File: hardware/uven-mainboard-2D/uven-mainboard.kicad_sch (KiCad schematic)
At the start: 38 parts, among them J1 TEMP_LED0, J10 TEMP_SPECIMEN, J11 TEC1_COOLER, J12 TEC2_COOLER, J13 DISPLAY, J14 DISPLAY, J15 TEC3_COOLER, J16 MENU_BUTTON, J18 BUTTON0, J19 BUTTON1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

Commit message: pcb ordered in aisler
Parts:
- removed J10: TEMP_SPECIMEN, Connector_PinSocket_1.27mm:PinSocket_1x02_P1.27mm_Vertical, symbol uven-mainboard-rescue:Conn_01x02_Female-Connector
- removed J8: TEMP_LED0, Connector_PinSocket_1.27mm:PinSocket_1x02_P1.27mm_Vertical, symbol uven-mainboard-rescue:Conn_01x02_Female-Connector
- removed J9: TEMP_LED1, Connector_PinSocket_1.27mm:PinSocket_1x02_P1.27mm_Vertical, symbol uven-mainboard-rescue:Conn_01x02_Female-Connector
- removed TH1, TH2, TH3: 10k, Resistor_SMD:R_0603_1608Metric_Pad1.05x0.95mm_HandSolder, symbol uven-mainboard-rescue:Thermistor_NTC-Device
- added H1, H4, H6: GND, MountingHole:MountingHole_3.2mm_M3_DIN965_Pad_TopBottom, symbol Mechanical:MountingHole_Pad
- added H2, H3, H5: 12V, MountingHole:MountingHole_3.2mm_M3_DIN965_Pad_TopBottom, symbol Mechanical:MountingHole_Pad
- added J10: LED1_CONTROL, Connector_PinHeader_2.54mm:PinHeader_1x05_P2.54mm_Vertical, symbol Connector:Conn_01x05_Male
- added J8: ST7789_ISP_DISPLAY, Connector_PinHeader_2.54mm:PinHeader_1x07_P2.54mm_Vertical, symbol Connector:Conn_01x07_Male
- added J9: LED0_CONTROL, Connector_PinHeader_2.54mm:PinHeader_1x05_P2.54mm_Vertical, symbol Connector:Conn_01x05_Male
- U1, U2, U3: footprint (none) -> custom_lib:BTS3011
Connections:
- net KILL_0 is gone; now on net KILL0: J22.2 (Pin_2)
- net TEMP_SPECISMEN is gone; now on net TEMP_SPECIMEN: J3.1 (Pin_1), R3.1
- net +12V: now also J4.2 (Pin_2), J5.2 (Pin_2), H2.1, H3.1, H5.1
- net +3V3: now also J10.2 (Pin_2), J8.2 (Pin_2), J9.2 (Pin_2)
- net GND: now also H1.1, H4.1, H6.1, J10.1 (Pin_1), J8.1 (Pin_1), J9.1 (Pin_1); no longer J4.1 (Pin_1), J5.1 (Pin_1)
- net KILL0: now also XA1.D28; no longer XA1.D38
- net MENU_BUTTON: now also XA1.D11
- net MENU_CLK: now also XA1.D13
- net MENU_DT: now also XA1.D12
- net TEC_COOLER_IN: now also XA1.D2; no longer XA1.D4 (D4_CS1)
- net TEC_COOLER_STATUS: now also XA1.D5; no longer XA1.D7
- net TEC_LED0_IN: now also XA1.D4 (D4_CS1); no longer XA1.D2
- net TEC_LED0_STATUS: now also XA1.D7; no longer XA1.D5
- net LED0_ON/OFF: now reaches XA1.D14 (D14_TX3)
- net LED0_ON/OFF: now also J9.5 (Pin_5)
- net LED1_ON/OFF: now reaches XA1.D15 (D15_RX3)
- net LED1_ON/OFF: now also J10.5 (Pin_5)
- net LED0_I2C_SDA: now reaches XA1.D20 (D20_SDA)
- net LED0_I2C_SDA: now also J9.4 (Pin_4)
- net LED0_I2C_SCL: now reaches XA1.D21 (D21_SCL)
- net LED0_I2C_SCL: now also J9.3 (Pin_3)
- net ISP_RES: now reaches XA1.D35
- net ISP_RES: now also J8.5 (Pin_5)
- net ISP_DC: now reaches XA1.D36
- net ISP_DC: now also J8.6 (Pin_6)
- net ISP_BLK: now reaches XA1.D37
- net ISP_BLK: now also J8.7 (Pin_7)
- net LED1_I2C_SCL: now reaches XA1.SCL1
- net LED1_I2C_SCL: now also J10.3 (Pin_3)
- net LED1_I2C_SDA: now reaches XA1.SDA1
- net LED1_I2C_SDA: now also J10.4 (Pin_4)
- net at J11.1 (Pin_1), J12.1 (Pin_1), J15.1 (Pin_1)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: no longer U2.3 (OUT)
- net MISO renamed SPI_MISO
- net MOSI renamed SPI_MOSI
- net SPI_MOSI: now also J8.4 (Pin_4)
- net SCK renamed SPI_SCK
- net SPI_SCK: now also J8.3 (Pin_3)
- new net: J5.1 (Pin_1), U3.6 (OUT)
- new net: J4.1 (Pin_1), U1.6 (OUT)
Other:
- moved on the sheet: J1, J14, J2, J3, J4, R1, R2, R3, XA1

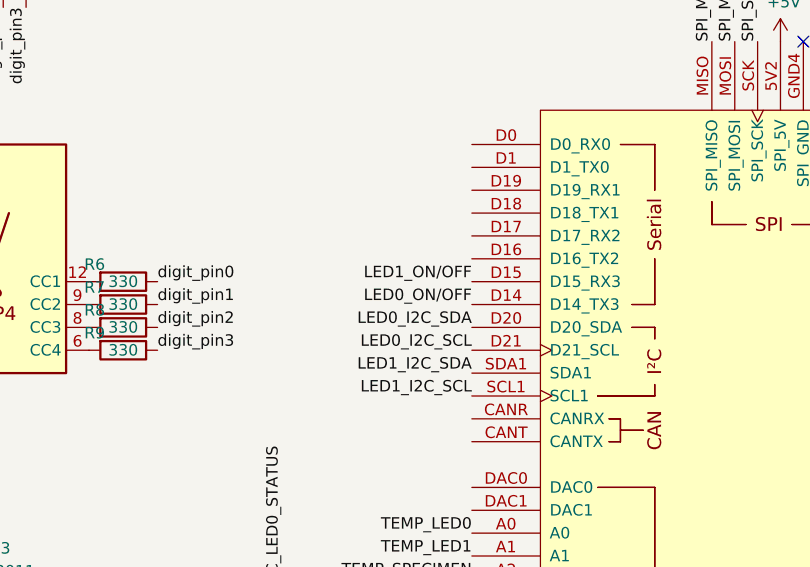
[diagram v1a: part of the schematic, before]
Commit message: uven pocket layout almost finished
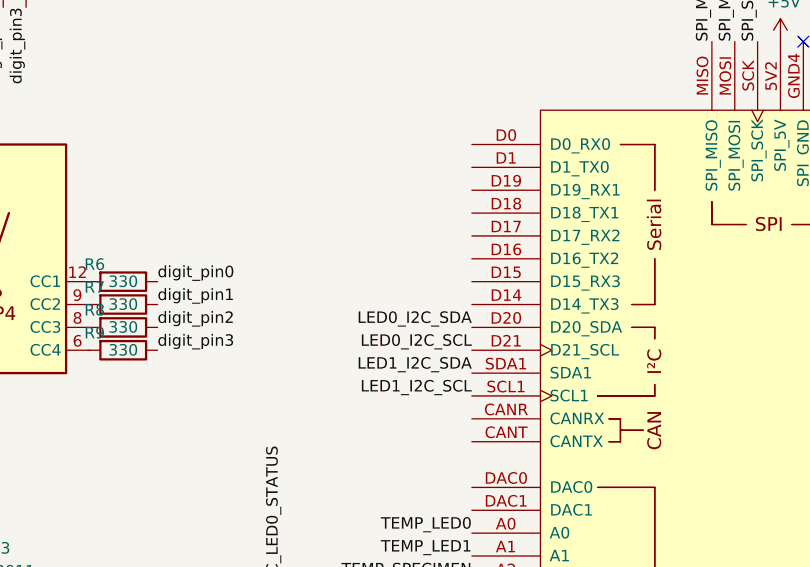
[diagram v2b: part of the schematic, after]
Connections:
- net LED0_ON/OFF: no longer XA1.D14 (D14_TX3)
- net LED1_ON/OFF: no longer XA1.D15 (D15_RX3)
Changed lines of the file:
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@@
     (effects (font (size 1.27 1.27)) (justify left bottom))
-  )
-  (label "LED0_ON{slash}OFF" (at 119.38 60.96 180)
-    (effects (font (size 1.27 1.27)) (justify right bottom))
   )
   (label "d" (at 20.955 55.88 180)
@@
     (effects (font (size 1.27 1.27)) (justify left bottom))
   )
-  (label "LED1_ON{slash}OFF" (at 119.38 58.42 180)
-    (effects (font (size 1.27 1.27)) (justify right bottom))
-  )
   (label "TEC_COOLER_IN" (at 185.42 43.18 0)
